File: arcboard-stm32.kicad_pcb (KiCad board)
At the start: 2 copper layers, 0 parts

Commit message: savegame jul23
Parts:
- added C1: 100nf, Capacitor_SMD:C_0402_1005Metric, F.Cu at (117.8, 52.1)
- added C10: 4.7uf, Capacitor_SMD:C_0402_1005Metric, F.Cu at (102.0, 92.4)
- added C12: 100nf, Capacitor_SMD:C_0402_1005Metric, F.Cu at (95.6, 92.2)
- added C13: 1u, kicad-libraries:C0402, F.Cu at (91.7, 74.4)
- added C15: 1u, kicad-libraries:C0402, F.Cu at (155.2, 92.1)
- added C18: 100nf, kicad-libraries:C0402, F.Cu at (61.3, 41.6)
- added C19: 100nf, kicad-libraries:C0402, F.Cu at (61.3, 43.7)
- added C2: 2.2uf, Capacitor_SMD:C_0402_1005Metric, F.Cu at (107.7, 81.8)
- added C27: 1u, kicad-libraries:C0402, F.Cu at (91.7, 76.9)
- added C3: 12p, Capacitor_SMD:C_0402_1005Metric, F.Cu at (96.2, 95.1)
- added C4: 2.2uf, Capacitor_SMD:C_0402_1005Metric, F.Cu at (96.5, 77.3)
- added C5: 100nf, Capacitor_SMD:C_0402_1005Metric, F.Cu at (94.8, 78.4)
- added C6: 12p, Capacitor_SMD:C_0402_1005Metric, F.Cu at (100.8, 97.1)
- added C7: 100nf, Capacitor_SMD:C_0402_1005Metric, F.Cu at (107.7, 80.8)
- added C8: 100nf, Capacitor_SMD:C_0402_1005Metric, F.Cu at (92.8, 88.6)
- added C9: 100nf, Capacitor_SMD:C_0402_1005Metric, F.Cu at (107.3, 88.0)
- added CYBOARD-MAIN1: ECT818001569, kicad-libraries:FPC-SMD_ECT818001569, F.Cu at (47.2, 74.3)
- added D2: B5817, Diode_SMD:D_SOD-323, F.Cu at (89.2, 73.3)
- added D4: SMF5_0CA_C364279, kicad-libraries:SOD-123FL_L2.8-W1.8-LS3.7-BI, F.Cu at (111.3, 66.1)
- added D5: USBLC6-2P6_C2827693, kicad-libraries:SOT-666-6_L1.6-W1.2-P0.50-LS1.6-BL, F.Cu at (111.4, 78.0)
- added D7: USBLC6-2P6_C2827693, kicad-libraries:SOT-666-6_L1.6-W1.2-P0.50-LS1.6-BL, F.Cu at (100.0, 73.2)
- added F1: Polyfuse, kicad-libraries:F1206, F.Cu at (89.6, 71.1)
- added F3: MF-NSMF075-2, kicad-libraries:F1206, F.Cu at (114.0, 66.1)
- added J1: Conn_01x02_Socket, Connector_PinSocket_2.54mm:PinSocket_1x02_P2.54mm_Vertical, F.Cu at (114.0, 50.8)
- added J13: ~, kicad-libraries:FFC-SMD_FFC05001-12SBA124W5M, F.Cu at (32.2, 105.2)
- added J14: ~, kicad-libraries:FFC-SMD_FFC05001-12SBA124W5M, F.Cu at (32.2, 113.6)
- added J15: ~, kicad-libraries:FFC-SMD_FFC05001-12SBA124W5M, F.Cu at (32.2, 122.0)
- added J16: ~, kicad-libraries:FFC-SMD_FFC05001-12SBA124W5M, F.Cu at (151.3, 84.8)
- added J3: ~, kicad-libraries:FFC-SMD_FFC05001-12SBA124W5M, F.Cu at (32.2, 63.1)
- added J4: ~, kicad-libraries:FFC-SMD_FFC05001-12SBA124W5M, F.Cu at (32.2, 71.5)
- added J6: ~, kicad-libraries:FFC-SMD_FFC05001-12SBA124W5M, F.Cu at (32.2, 79.9)
- added J7: ~, kicad-libraries:FFC-SMD_FFC05001-12SBA124W5M, F.Cu at (32.2, 88.3)
- added J8: ~, kicad-libraries:FFC-SMD_FFC05001-12SBA124W5M, F.Cu at (32.2, 96.8)
- added JP2: SolderJumper_3_Open, Jumper:SolderJumper-3_P1.3mm_Open_Pad1.0x1.5mm, F.Cu at (108.7, 66.2)
- added JP3: SolderJumper_3_Open, Jumper:SolderJumper-3_P1.3mm_Open_Pad1.0x1.5mm, F.Cu at (88.3, 40.5)
- added L1: MPZ2012S101AT000, kicad-libraries:L0805, F.Cu at (112.5, 70.0)
- added LED-LVL1: SN74LVC1T45DRL, kicad-libraries:SOT-563_L1.6-W1.2-P0.50-LS1.6-BR, F.Cu at (56.9, 42.1)
- added MOSFET1: AO3401A_C347476, kicad-libraries:SOT-23_L2.9-W1.3-P1.90-LS2.4-BR, F.Cu at (108.7, 71.0)
- added R1: 10k, Resistor_SMD:R_0402_1005Metric, F.Cu at (116.5, 54.6)
- added R10: 5.1k, Resistor_SMD:R_0402_1005Metric, F.Cu at (90.6, 69.2)
- added R11: 10k, Resistor_SMD:R_0402_1005Metric, F.Cu at (89.0, 68.8)
- added R12: 10k, Resistor_SMD:R_0402_1005Metric, F.Cu at (83.8, 40.2)
- added R20: 10k, Resistor_SMD:R_0402_1005Metric, F.Cu at (83.8, 42.1)
- added R4: 5.1k, Resistor_SMD:R_0402_1005Metric, F.Cu at (101.5, 73.2)
- added R5: 5.1k, Resistor_SMD:R_0402_1005Metric, F.Cu at (98.4, 73.1)
- added U1: XC6210B332MR-G, Package_TO_SOT_SMD:SOT-23-5, F.Cu at (94.1, 75.2)
- added U2: TYPE-C-31-M-13, kicad-libraries:USB-C_SMD-TYPE-C-31-M-12, F.Cu at (100.0, 67.8)
- added U3: STM32F405RGTx, Package_QFP:LQFP-64_10x10mm_P0.5mm, F.Cu at (100.0, 85.0)
- added U4: PJ-320A, kicad-libraries:AUDIO-TH_XKB_PJ-320A, F.Cu at (120.0, 71.8)
- added U5: BAV70S,115, kicad-libraries:SOT-363-6_L2.0-W1.3-P0.65-LS2.1-BL, F.Cu at (40.5, 62.3)
- added U6: BAV70S,115, kicad-libraries:SOT-363-6_L2.0-W1.3-P0.65-LS2.1-BL, F.Cu at (44.2, 62.3)
- added U7: BAV70S,115, kicad-libraries:SOT-363-6_L2.0-W1.3-P0.65-LS2.1-BL, F.Cu at (48.0, 62.3)
- added U8: BAV70S,115, kicad-libraries:SOT-363-6_L2.0-W1.3-P0.65-LS2.1-BL, F.Cu at (51.7, 62.3)
- added U9: BAV70S,115, kicad-libraries:SOT-363-6_L2.0-W1.3-P0.65-LS2.1-BL, F.Cu at (55.5, 62.3)
- added Y1: Crystal_GND24, kicad-libraries:CRYSTAL-SMD_4P-L3.2-W2.5-BL-1, F.Cu at (98.5, 95.7)
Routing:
- net GND: track 0.00 -> 75.9 mm, vias 0 -> 16
- net +3V3: track 0.00 -> 59.4 mm, vias 0 -> 1
- net USB_CONN_DP: track 0.00 -> 14.8 mm
- net USB_CONN_DM: track 0.00 -> 12.2 mm, vias 0 -> 2
- net VBUS: track 0.00 -> 10.4 mm
- net +5V: track 0.00 -> 9.52 mm, vias 0 -> 2
- net PH1: track 0.00 -> 9.26 mm
- net PH0: track 0.00 -> 6.92 mm
- net SourceSinkPulldown: track 0.00 -> 4.99 mm
- net Net-(D2-A): track 0.00 -> 2.23 mm
- net Net-(U3-VCAP_2): track 0.00 -> 1.65 mm
- net Net-(U3-VCAP_1): track 0.00 -> 1.58 mm
- net VBUS_DETECT: track 0.00 -> 1.03 mm
- added copper zone on B.Cu, net GND
- added copper zone on F.Cu, net GND
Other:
- board outline added: 75 x 75 mm

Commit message: mostly there
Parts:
- added C11: 100nf, Capacitor_SMD:C_0402_1005Metric, F.Cu at (101.9, 92.3)
- added C14: 100nf, Capacitor_SMD:C_0402_1005Metric, F.Cu at (89.3, 90.6)
- added C16: 100nf, Capacitor_SMD:C_0402_1005Metric, F.Cu at (91.5, 99.7)
- added C17: 100nf, Capacitor_SMD:C_0402_1005Metric, F.Cu at (93.2, 98.0)
- added C20: 4.7uf, Capacitor_SMD:C_0402_1005Metric, F.Cu at (96.7, 103.1)
- added H1: MountingHole, MountingHole:MountingHole_3.2mm_M3_Pad_Via, F.Cu at (66.5, 66.5)
- added H2: MountingHole, MountingHole:MountingHole_3.2mm_M3_Pad_Via, F.Cu at (118.0, 66.5)
- added H3: MountingHole, MountingHole:MountingHole_3.2mm_M3_Pad_Via, F.Cu at (118.0, 118.2)
- added H4: MountingHole, MountingHole:MountingHole_3.2mm_M3_Pad_Via, F.Cu at (66.5, 118.2)
- added J10: Conn_01x02_Socket, Connector_PinSocket_1.27mm:PinSocket_1x02_P1.27mm_Vertical, F.Cu at (82.7, 78.8)
- added J2: Conn_01x02_Socket, Connector_PinSocket_1.27mm:PinSocket_1x02_P1.27mm_Vertical, F.Cu at (88.5, 97.2)
- added J5: Conn_01x02_Socket, Connector_PinSocket_1.27mm:PinSocket_1x02_P1.27mm_Vertical, F.Cu at (88.5, 92.3)
- added J9: Conn_01x03_Socket, Connector_PinHeader_2.54mm:PinHeader_1x03_P2.54mm_Vertical, F.Cu at (81.7, 110.4)
- added R2: 1k, Resistor_SMD:R_0402_1005Metric, F.Cu at (91.5, 98.7)
- added REF1: SN74AHC1G14DRLR, kicad-libraries:SOT-553-5_L1.6-W1.2-P0.50-LS1.6-BL, F.Cu at (91.6, 96.8)
- added U10: 1N4148W_C81598, kicad-libraries:SOD-123F_L2.7-W1.6-LS3.8-RD, F.Cu at (91.3, 92.9)
- C1: value 100nf -> 4.7uf; footprint Capacitor_SMD:C_0402_1005Metric -> Capacitor_SMD:C_0805_2012Metric
- J1: footprint Connector_PinSocket_2.54mm:PinSocket_1x02_P2.54mm_Vertical -> Connector_PinSocket_1.27mm:PinSocket_1x02_P1.27mm_Vertical
- R1: value 10k -> 75k
- moved J15 85.9 mm to (115.0, 91.0), turned to 90 degrees
- moved J14 84.4 mm to (115.0, 106.0), turned to 90 degrees
- moved J3 83.8 mm to (115.0, 76.0), turned to 90 degrees
- moved C1 71.6 mm to (85.0, 115.8)
- moved J13 61.1 mm to (92.5, 115.0)
- moved CYBOARD-MAIN1 58.4 mm to (96.1, 106.2)
- moved J1 55.0 mm to (88.5, 99.5)
- moved C15 53.9 mm to (105.2, 112.2), turned to 0 degrees
- moved J16 53.2 mm to (107.5, 115.0)
- moved R1 52.7 mm to (91.5, 101.0), turned to 180 degrees
- moved U5 51.1 mm to (76.5, 98.5), turned to -90 degrees
- moved U9 50.5 mm to (77.2, 107.9), turned to -90 degrees
- moved LED-LVL1 50.2 mm to (78.9, 87.1), turned to -90 degrees
- moved U8 49.6 mm to (77.2, 104.8), turned to -90 degrees
- moved J8 48.9 mm to (77.5, 115.0)
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- renumbered J15 to J14, J14 to J15
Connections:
- C1 pad 1: NRST -> +5V
- D7 pad 1: USB_CONN_DM -> USB_DM
- D7 pad 3: USB_CONN_DP -> USB_DP
- J14 pad 7: ENCODER2-r1 -> ENCODER1_R1
- J14 pad 9: ENCODER2-r2 -> ENCODER1_R2
- J15 pad 7: ENCODER1-r1 -> ENCODER2_R1
- J15 pad 9: ENCODER1-r2 -> ENCODER2_R2
- J16 pad 10: LCD1_CS -> LCD_CS
- J3 pad 7: ENCODER3-r1 -> ENCODER3_R1
- J3 pad 9: ENCODER3-r2 -> ENCODER3_R2
- J6 pad 4: LED_KEYS_DI -> LED_DPAD_DI
- U3 pad 10: unconnected-(U3-PC2-Pad10) -> ROW2
- U3 pad 11: unconnected-(U3-PC3-Pad11) -> ROW3
- U3 pad 14: unconnected-(U3-PA0-Pad14) -> ROW4
- U3 pad 15: unconnected-(U3-PA1-Pad15) -> ROW5
- U3 pad 16: unconnected-(U3-PA2-Pad16) -> ROW6
- U3 pad 17: unconnected-(U3-PA3-Pad17) -> ROW7
- U3 pad 2: unconnected-(U3-PC13-Pad2) -> COL3
- U3 pad 21: SPI1_SCK -> SPI1_CLK
- U3 pad 24: unconnected-(U3-PC4-Pad24) -> PMW_CS
- U3 pad 25: unconnected-(U3-PC5-Pad25) -> LCD_CS
- U3 pad 26: unconnected-(U3-PB0-Pad26) -> LCD_DC
- U3 pad 27: unconnected-(U3-PB1-Pad27) -> LCD_RST
- U3 pad 28: unconnected-(U3-PB2-Pad28) -> LCD_BL
- U3 pad 3: unconnected-(U3-PC14-Pad3) -> COL2
- U3 pad 34: unconnected-(U3-PB13-Pad34) -> ENCODER3_R2
- U3 pad 35: unconnected-(U3-PB14-Pad35) -> ENCODER3_R1
- U3 pad 36: unconnected-(U3-PB15-Pad36) -> ENCODER2_R2
- U3 pad 37: unconnected-(U3-PC6-Pad37) -> ENCODER2_R1
- U3 pad 38: unconnected-(U3-PC7-Pad38) -> ENCODER1_R2
- U3 pad 39: unconnected-(U3-PC8-Pad39) -> ENCODER1_R1
- U3 pad 4: unconnected-(U3-PC15-Pad4) -> COL1
- U3 pad 40: unconnected-(U3-PC9-Pad40) -> SPLIT_HAND
- U3 pad 44: USB_CONN_DM -> USB_DM
- U3 pad 45: USB_CONN_DP -> USB_DP
- U3 pad 46: unconnected-(U3-PA13-Pad46) -> SWDIO
- U3 pad 49: unconnected-(U3-PA14-Pad49) -> SWCLK
- U3 pad 50: unconnected-(U3-PA15-Pad50) -> COL10
- U3 pad 51: unconnected-(U3-PC10-Pad51) -> COL9
- U3 pad 52: unconnected-(U3-PC11-Pad52) -> COL8
- U3 pad 53: unconnected-(U3-PC12-Pad53) -> COL7
- U3 pad 55: unconnected-(U3-PB3-Pad55) -> COL6
- U3 pad 56: unconnected-(U3-PB4-Pad56) -> COL11
- U3 pad 57: unconnected-(U3-PB5-Pad57) -> COL12
- U3 pad 58: unconnected-(U3-PB6-Pad58) -> COL13
- U3 pad 59: unconnected-(U3-PB7-Pad59) -> COL4
- U3 pad 61: unconnected-(U3-PB8-Pad61) -> COL5
- U3 pad 62: unconnected-(U3-PB9-Pad62) -> COL0
- U3 pad 8: unconnected-(U3-PC0-Pad8) -> ROW0
- U3 pad 9: unconnected-(U3-PC1-Pad9) -> ROW1
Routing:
- net +5V: track 9.52 -> 238.5 mm, vias 2 -> 22
- net +3V3: track 59.4 -> 265.9 mm, vias 1 -> 18
- net GND: track 75.9 -> 222.3 mm, vias 16 -> 148
- net ROW5: track 0.00 -> 117.3 mm, vias 0 -> 10
- net ROW6: track 0.00 -> 96.0 mm, vias 0 -> 9
- net ROW4: track 0.00 -> 71.1 mm, vias 0 -> 7
- net COL10: track 0.00 -> 67.1 mm, vias 0 -> 11
- net COL7: track 0.00 -> 65.8 mm, vias 0 -> 7
- net LED_DPAD_DI: track 0.00 -> 61.7 mm, vias 0 -> 8
- net Net-(J8-GP_AD1): track 0.00 -> 56.5 mm, vias 0 -> 4
- net SPI1_CLK: track 0.00 -> 53.5 mm, vias 0 -> 6
- net SPI1_MOSI: track 0.00 -> 52.7 mm, vias 0 -> 5
- net COL6: track 0.00 -> 51.5 mm, vias 0 -> 5
- net PMW_CS: track 0.00 -> 50.6 mm, vias 0 -> 6
- net ENCODER1_R1: track 0.00 -> 48.6 mm, vias 0 -> 2
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- added copper zone on F.Cu, net +5V
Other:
- board size 75 x 75 mm -> 59.5 x 59.7 mm
- board text added: "5V"
- board text added: "BOOT"
- board text added: "BYPASS"
- board text added: "DFU"
- board text added: "DPAD1"
- board text added: "DPAD2"
- board text added: "DPAD3"
- board text added: "DPAD4"
- board text added: "ENCODER1"
- board text added: "ENCODER2"
- board text added: "ENCODER3"
- board text added: "GND"
- board text added: "LCD"
- board text added: "LED"
- board text added: "LEFT"
- board text added: "PMW"
- board text added: "RESET"

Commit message: savegame
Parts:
- added R7: 10k, Resistor_SMD:R_0402_1005Metric, F.Cu at (76.3, 81.2)
- added R8: 10k, Resistor_SMD:R_0402_1005Metric, F.Cu at (106.1, 107.6)
- added U12: AO3401A, kicad-libraries:SOT-23_L2.9-W1.3-P1.90-LS2.4-BR, F.Cu at (105.6, 109.8)
- added U13: AO3401A, kicad-libraries:SOT-23_L2.9-W1.3-P1.90-LS2.4-BR, F.Cu at (75.4, 84.0)
- moved C9 0.25 mm to (107.3, 88.3)
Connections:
- C1 pad 1: +5V -> RGB_5V
- C15 pad 1: +3V3 -> LCD_3V3
- C20 pad 2: +5V -> RGB_5V
- CYBOARD-MAIN1 pad 13: +5V -> RGB_5V
- CYBOARD-MAIN1 pad 14: +5V -> RGB_5V
- CYBOARD-MAIN1 pad 15: +5V -> RGB_5V
- CYBOARD-MAIN1 pad 16: +5V -> RGB_5V
- J13 pad 13: (no net) -> GND
- J13 pad 14: (no net) -> GND
- J14 pad 13: (no net) -> GND
- J14 pad 14: (no net) -> GND
- J15 pad 13: (no net) -> GND
- J15 pad 14: (no net) -> GND
- J16 pad 1: +3V3 -> LCD_3V3
- J16 pad 13: (no net) -> GND
- J16 pad 14: (no net) -> GND
- J16 pad 6: +5V -> unconnected-(J16-5V-Pad6)
- J3 pad 13: (no net) -> GND
- J3 pad 14: (no net) -> GND
- J4 pad 13: (no net) -> GND
- J4 pad 14: (no net) -> GND
- J4 pad 3: +5V -> RGB_5V
- J6 pad 13: (no net) -> GND
- J6 pad 14: (no net) -> GND
- J6 pad 3: +5V -> RGB_5V
- J7 pad 13: (no net) -> GND
- J7 pad 14: (no net) -> GND
- J7 pad 3: +5V -> RGB_5V
- J8 pad 13: (no net) -> GND
- J8 pad 14: (no net) -> GND
- J8 pad 3: +5V -> RGB_5V
- J9 pad 2: +5V -> RGB_5V
- U3 pad 29: unconnected-(U3-PB10-Pad29) -> LCD_ON
- U3 pad 33: unconnected-(U3-PB12-Pad33) -> SPLIT_HAND
- U3 pad 40: SPLIT_HAND -> RGB_ON
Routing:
- net +5V: track 238.5 -> 63.5 mm, vias 22 -> 6
- net RGB_5V: track 0.00 -> 164.3 mm, vias 0 -> 16
- net RGB_ON: track 0.00 -> 58.8 mm, vias 0 -> 2
- net LCD_ON: track 0.00 -> 36.5 mm, vias 0 -> 2
- net unconnected-(U3-PB11-Pad30): track 3.78 -> 29.1 mm, vias 0 -> 1
- net GND: track 222.3 -> 235.7 mm, vias 148 -> 144
- net LED_SIG_OUTPUT: track 41.0 -> 31.7 mm, vias 6 -> 4
- net LCD_3V3: track 0.00 -> 6.55 mm
- net +3V3: track 265.9 -> 272.3 mm, vias 18 -> 19
- net unconnected-(U3-PB12-Pad33): track 6.05 -> 0.00 mm, vias 1 -> 0
- net unconnected-(U3-PB10-Pad29): track 3.55 -> 0.00 mm
- net SPLIT_HAND: track 19.1 -> 16.4 mm
- net SPI1_CLK: track 53.5 -> 51.8 mm
- net unconnected-(U3-PA4-Pad20): track 3.25 -> 2.22 mm
- net SERIAL_TX: track 42.0 -> 41.2 mm
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
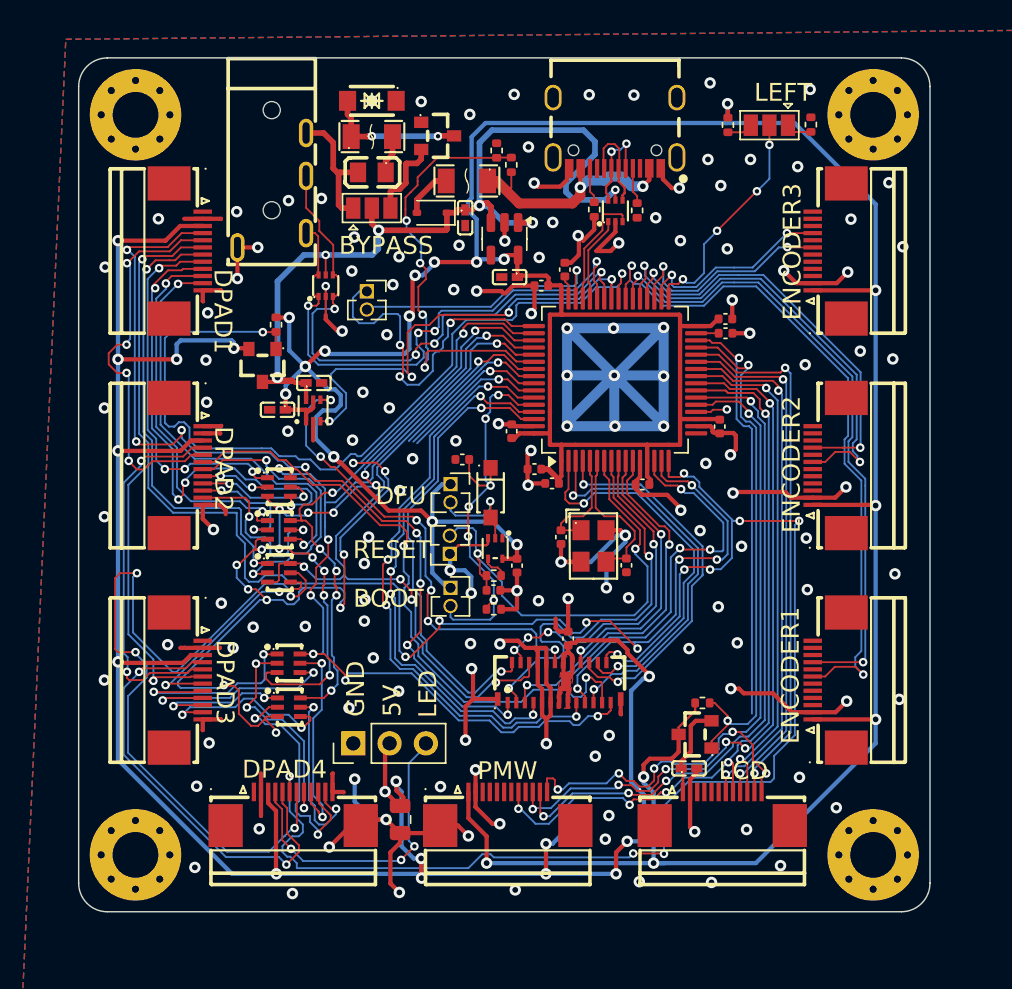
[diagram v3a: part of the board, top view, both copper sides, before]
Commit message: cleaned up routing quite a bit
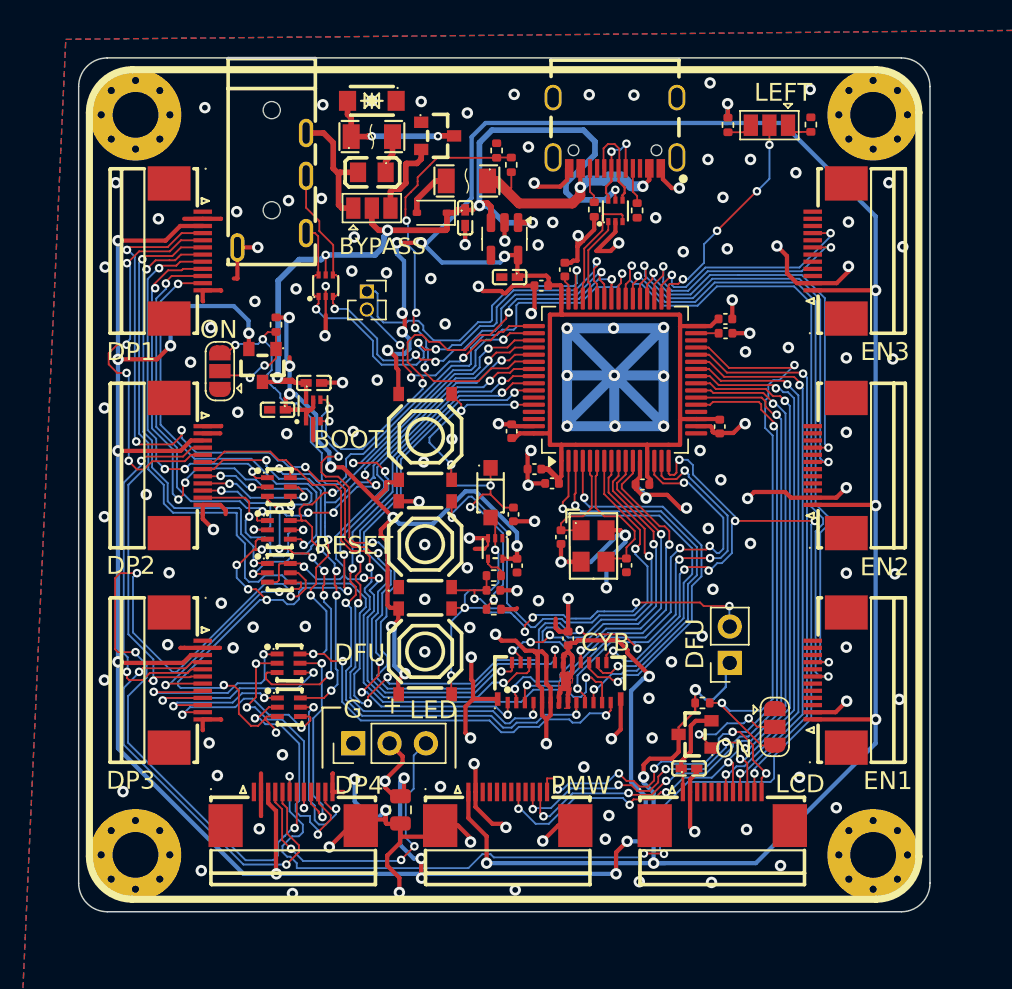
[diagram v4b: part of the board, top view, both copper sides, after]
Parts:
- removed J1, J2: Conn_01x02_Socket, Connector_PinSocket_1.27mm:PinSocket_1x02_P1.27mm_Vertical
- added JP1: SolderJumper_3_Open, Jumper:SolderJumper-3_P1.3mm_Open_RoundedPad1.0x1.5mm, F.Cu at (72.4, 84.4)
- added JP4: SolderJumper_3_Open, Jumper:SolderJumper-3_P1.3mm_Open_RoundedPad1.0x1.5mm, F.Cu at (111.2, 109.3)
- added U11: TS-1187A-B-A-B, kicad-libraries:SW-SMD_4P-L5.1-W5.1-P3.70-LS6.5-TL_H1.5, F.Cu at (86.7, 89.0)
- added U14: TS-1187A-B-A-B, kicad-libraries:SW-SMD_4P-L5.1-W5.1-P3.70-LS6.5-TL_H1.5, F.Cu at (86.7, 96.5)
- added U15: TS-1187A-B-A-B, kicad-libraries:SW-SMD_4P-L5.1-W5.1-P3.70-LS6.5-TL_H1.5, F.Cu at (86.7, 104.0)
- J5: footprint Connector_PinSocket_1.27mm:PinSocket_1x02_P1.27mm_Vertical -> Connector_PinSocket_2.54mm:PinSocket_1x02_P2.54mm_Vertical
- moved J5 23.2 mm to (108.0, 104.8), turned to 180 degrees
- moved C14 5.25 mm to (92.9, 94.4), turned to -90 degrees
- moved C1 0.68 mm to (85.0, 115.1)
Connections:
- J10 pad 1: SWCLK -> SWDIO
- J10 pad 2: SWDIO -> SWCLK
- U12 pad 1: LCD_ON -> Net-(JP4-C)
- U13 pad 1: RGB_ON -> Net-(JP1-C)
- U3 pad 17: ROW7 -> unconnected-(U3-PA3-Pad17)
- U3 pad 56: COL11 -> COL4
- U3 pad 57: COL12 -> COL5
- U3 pad 58: COL13 -> COL0
- U3 pad 59: COL4 -> unconnected-(U3-PB7-Pad59)
- U3 pad 61: COL5 -> unconnected-(U3-PB8-Pad61)
- U3 pad 62: COL0 -> unconnected-(U3-PB9-Pad62)
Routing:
- net Net-(J5-Pin_2): track 6.95 -> 38.2 mm, vias 1 -> 7
- net unconnected-(U3-PB11-Pad30): track 29.1 -> 0.00 mm, vias 1 -> 0
- net +3V3: track 272.3 -> 286.6 mm, vias 19 -> 22
- net COL11: track 11.4 -> 0.00 mm, vias 1 -> 0
- net COL12: track 10.8 -> 0.00 mm, vias 1 -> 0
- net COL13: track 10.3 -> 0.00 mm, vias 1 -> 0
- net RGB_ON: track 58.8 -> 49.7 mm, vias 2 -> 3
- net NRST: track 32.9 -> 41.7 mm, vias 2 -> 3
- net SWCLK: track 23.9 -> 16.1 mm
- net COL0: track 32.5 -> 40.2 mm
- net Net-(JP4-C): track 0.00 -> 7.36 mm, vias 0 -> 2
- net LED_KEYS_DI: track 34.1 -> 41.3 mm, vias 6 -> 4
- net COL4: track 42.5 -> 49.4 mm
- net ROW5: track 117.3 -> 124.0 mm
- net COL5: track 38.1 -> 44.8 mm
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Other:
- board text added: "+"
- board text added: "CYB"
- board text added: "DP1"
- board text added: "DP2"
- board text added: "DP3"
- board text added: "DP4"
- board text added: "EN1"
- board text added: "EN2"
- board text added: "EN3"
- board text added: "G"
- board text added: "ON"
- board text removed: "5V"
- board text removed: "DPAD1"
- board text removed: "DPAD2"
- board text removed: "DPAD3"
- board text removed: "DPAD4"
- board text removed: "ENCODER1"
- board text removed: "ENCODER2"
- board text removed: "ENCODER3"
- board text removed: "GND"
